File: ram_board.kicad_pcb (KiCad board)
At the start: 2 copper layers, 28.6 x 73 mm, 6 parts, among them J1 Conn_02x20_Odd_Even, J2 Conn_02x05_Odd_Even, U1 IS61LV5128AL-10TLI, U2 SST39VF040-70-4C-NHE

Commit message: Wiring up
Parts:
- added C1: 100nF, Capacitor_SMD:C_0603_1608Metric_Pad1.05x0.95mm_HandSolder, B.Cu at (173.5, 74.8)
- added C2: 100nF, Capacitor_SMD:C_0603_1608Metric_Pad1.05x0.95mm_HandSolder, F.Cu at (142.2, 84.6)
- added C3: 100nF, Capacitor_SMD:C_0603_1608Metric_Pad1.05x0.95mm_HandSolder, F.Cu at (124.1, 90.7)
- added C4: 100uF, Capacitor_SMD:C_1206_3216Metric_Pad1.42x1.75mm_HandSolder, F.Cu at (124.2, 94.0)
- added G***: LOGO, Logos:asian_tiger, F.Cu at (160.8, 85.5)
- added R2: 10K, Resistor_SMD:R_0603_1608Metric_Pad1.05x0.95mm_HandSolder, B.Cu at (177.0, 74.8)
- D1: footprint LED_SMD:LED_0805_2012Metric_Pad1.15x1.40mm_HandSolder -> LED_SMD:LED_0603_1608Metric_Pad1.05x0.95mm_HandSolder
- R1: footprint Resistor_SMD:R_0805_2012Metric_Pad1.15x1.40mm_HandSolder -> Resistor_SMD:R_0603_1608Metric_Pad1.05x0.95mm_HandSolder
- moved U2 39.3 mm to (174.4, 83.9)
- moved U1 38.2 mm to (151.3, 84.1)
- moved J2 30.1 mm to (119.0, 97.5), turned to 90 degrees
- moved J1 18.4 mm to (140.1, 97.7), turned to 90 degrees
- moved R1 11.6 mm to (132.0, 77.0), turned to 180 degrees
- moved D1 4.65 mm to (137.6, 77.0), turned to 180 degrees
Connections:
- J1 pad 1: (no net) -> /A0
- J1 pad 10: (no net) -> /A9
- J1 pad 11: (no net) -> /A10
- J1 pad 12: (no net) -> /A11
- J1 pad 13: (no net) -> /A12
- J1 pad 14: (no net) -> /A13
- J1 pad 15: (no net) -> /A14
- J1 pad 16: (no net) -> /A15
- J1 pad 17: (no net) -> /A16
- J1 pad 18: (no net) -> /A17
- J1 pad 19: (no net) -> /A18
- J1 pad 2: (no net) -> /A1
- J1 pad 21: (no net) -> /RAM_CE
- J1 pad 22: (no net) -> /D0
- J1 pad 23: (no net) -> /RAM_OE
- J1 pad 24: (no net) -> /D1
- J1 pad 25: (no net) -> /RAM_WE
- J1 pad 26: (no net) -> /D2
- J1 pad 28: (no net) -> /D3
- J1 pad 3: (no net) -> /A2
- J1 pad 32: (no net) -> GND
- J1 pad 33: (no net) -> GND
- J1 pad 34: (no net) -> /D4
- J1 pad 36: (no net) -> /D5
- J1 pad 38: (no net) -> /D6
- J1 pad 39: (no net) -> GND
- J1 pad 4: (no net) -> /A3
- J1 pad 40: (no net) -> /D7
- J1 pad 5: (no net) -> /A4
- J1 pad 6: (no net) -> /A5
- J1 pad 7: (no net) -> /A6
- J1 pad 8: (no net) -> /A7
- J1 pad 9: (no net) -> /A8
- J2 pad 10: (no net) -> GND
- J2 pad 3: (no net) -> +3V3
- J2 pad 4: (no net) -> +3V3
- J2 pad 7: (no net) -> GND
- J2 pad 8: (no net) -> GND
- J2 pad 9: (no net) -> GND
- R1 pad 2: (no net) -> +3V3
- U1 pad 10: (no net) -> /D1
- U1 pad 11: Net-(U1-Pad11) -> +3V3
- U1 pad 12: Net-(U1-Pad12) -> GND
- U1 pad 13: (no net) -> /D2
- U1 pad 14: (no net) -> /D3
- U1 pad 15: (no net) -> /RAM_WE
- U1 pad 16: (no net) -> /A5
- U1 pad 17: (no net) -> /A6
- U1 pad 18: (no net) -> /A7
- U1 pad 19: (no net) -> /A8
- U1 pad 20: (no net) -> /A9
- U1 pad 26: (no net) -> /A10
- U1 pad 27: (no net) -> /A11
- U1 pad 28: (no net) -> /A12
- U1 pad 29: (no net) -> /A13
- U1 pad 3: (no net) -> /A0
- U1 pad 30: (no net) -> /A14
- U1 pad 31: (no net) -> /D4
- U1 pad 32: (no net) -> /D5
- U1 pad 33: Net-(U1-Pad11) -> +3V3
- U1 pad 34: Net-(U1-Pad12) -> GND
- U1 pad 35: (no net) -> /D6
- U1 pad 36: (no net) -> /D7
- U1 pad 37: (no net) -> /RAM_OE
- U1 pad 38: (no net) -> /A15
- U1 pad 39: (no net) -> /A16
- U1 pad 4: (no net) -> /A1
- U1 pad 40: (no net) -> /A17
- U1 pad 41: (no net) -> /A18
- U1 pad 5: (no net) -> /A2
- U1 pad 6: (no net) -> /A3
- U1 pad 7: (no net) -> /A4
- U1 pad 8: (no net) -> /RAM_CE
- U1 pad 9: (no net) -> /D0
- U2 pad 1: (no net) -> /A18
- U2 pad 10: (no net) -> /A2
- U2 pad 11: (no net) -> /A1
- U2 pad 12: (no net) -> /A0
- U2 pad 13: (no net) -> /D0
- U2 pad 14: (no net) -> /D1
- U2 pad 15: (no net) -> /D2
- U2 pad 17: (no net) -> /D3
- U2 pad 18: (no net) -> /D4
- U2 pad 19: (no net) -> /D5
- U2 pad 2: (no net) -> /A16
- U2 pad 20: (no net) -> /D6
- U2 pad 21: (no net) -> /D7
- U2 pad 22: (no net) -> /RAM_CE
- U2 pad 23: (no net) -> /A10
- U2 pad 24: (no net) -> /RAM_OE
- U2 pad 25: (no net) -> /A11
- U2 pad 26: (no net) -> /A9
- U2 pad 27: (no net) -> /A8
- U2 pad 28: (no net) -> /A13
- U2 pad 29: (no net) -> /A14
- U2 pad 3: (no net) -> /A15
- U2 pad 30: (no net) -> /A17
- U2 pad 31: (no net) -> Net-(R2-Pad1)
- U2 pad 32: (no net) -> +3V3
- U2 pad 4: (no net) -> /A12
- U2 pad 5: (no net) -> /A7
- U2 pad 6: (no net) -> /A6
- U2 pad 7: (no net) -> /A5
- U2 pad 8: (no net) -> /A4
- U2 pad 9: (no net) -> /A3
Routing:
- added copper zone on B.Cu, net GND
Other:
- board size 28.6 x 73 mm -> 73 x 31.6 mm
- rule trace_min: 0.2 -> 0.1524
- rule via_min_drill: 0.3 -> 0.3302
- rule via_min_size: 0.4 -> 0.6858

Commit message: more cowbell
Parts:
- moved C2 6.38 mm to (148.6, 84.0), turned to 270 degrees
- moved D1 2.17 mm to (135.4, 77.0)
- moved C4 0.22 mm to (124.0, 94.0)
- moved C3 0.11 mm to (124.0, 90.7)
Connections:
- J1 pad 20: (no net) -> Net-(J1-Pad20)
- J1 pad 22: /D0 -> Net-(J1-Pad22)
- J1 pad 24: /D1 -> Net-(J1-Pad24)
- J1 pad 26: /D2 -> Net-(J1-Pad26)
- J1 pad 27: (no net) -> /D0
- J1 pad 28: /D3 -> Net-(J1-Pad28)
- J1 pad 29: (no net) -> /D1
- J1 pad 30: (no net) -> /D2
- J1 pad 31: (no net) -> /D3
- J1 pad 35: (no net) -> /D6
- J1 pad 37: (no net) -> /ROM_CE
- J1 pad 38: /D6 -> /D7
- J1 pad 40: /D7 -> /ROM_OE
- J2 pad 1: (no net) -> Net-(J2-Pad1)
- J2 pad 2: (no net) -> Net-(J2-Pad2)
- J2 pad 5: (no net) -> Net-(J2-Pad5)
- J2 pad 6: (no net) -> Net-(J2-Pad6)
- U1 pad 1: (no net) -> Net-(U1-Pad1)
- U1 pad 2: (no net) -> Net-(U1-Pad2)
- U1 pad 21: (no net) -> Net-(U1-Pad21)
- U1 pad 22: (no net) -> Net-(U1-Pad22)
- U1 pad 23: (no net) -> Net-(U1-Pad23)
- U1 pad 24: (no net) -> Net-(U1-Pad24)
- U1 pad 25: (no net) -> Net-(U1-Pad25)
- U1 pad 42: (no net) -> Net-(U1-Pad42)
- U1 pad 43: (no net) -> Net-(U1-Pad43)
- U1 pad 44: (no net) -> Net-(U1-Pad44)
- U2 pad 22: /RAM_CE -> /ROM_CE
- U2 pad 24: /RAM_OE -> /ROM_OE
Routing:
- net +3V3: track 0.00 -> 101.4 mm, vias 0 -> 2
- net /A3: track 0.00 -> 65.4 mm, vias 0 -> 4
- net /A1: track 0.00 -> 65.1 mm, vias 0 -> 4
- net /A8: track 0.00 -> 64.9 mm, vias 0 -> 4
- net /A9: track 0.00 -> 63.8 mm, vias 0 -> 4
- net /A0: track 0.00 -> 63.2 mm, vias 0 -> 4
- net /A2: track 0.00 -> 61.3 mm, vias 0 -> 4
- net /A4: track 0.00 -> 60.7 mm, vias 0 -> 4
- net /A5: track 0.00 -> 58.7 mm, vias 0 -> 4
- net /A7: track 0.00 -> 58.7 mm, vias 0 -> 4
- net /A6: track 0.00 -> 54.8 mm, vias 0 -> 4
- net /A13: track 0.00 -> 47.7 mm, vias 0 -> 4
- net /A15: track 0.00 -> 45.3 mm, vias 0 -> 4
- net /A11: track 0.00 -> 45.1 mm, vias 0 -> 2
- net /A10: track 0.00 -> 44.4 mm, vias 0 -> 4
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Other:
- rule via_min_drill: 0.3302 -> 0.3048
- rule via_min_size: 0.6858 -> 0.635

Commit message: finished routing, gerbers
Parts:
- C2: moved to B.Cu
- moved G*** 11.5 mm to (149.5, 87.6)
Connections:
- J1 pad 20: Net-(J1-Pad20) -> (no net)
- J1 pad 22: Net-(J1-Pad22) -> (no net)
- J1 pad 24: Net-(J1-Pad24) -> (no net)
- J1 pad 26: Net-(J1-Pad26) -> (no net)
- J1 pad 28: Net-(J1-Pad28) -> (no net)
- J2 pad 1: Net-(J2-Pad1) -> (no net)
- J2 pad 2: Net-(J2-Pad2) -> (no net)
- J2 pad 5: Net-(J2-Pad5) -> (no net)
- J2 pad 6: Net-(J2-Pad6) -> (no net)
- U1 pad 1: Net-(U1-Pad1) -> (no net)
- U1 pad 2: Net-(U1-Pad2) -> (no net)
- U1 pad 21: Net-(U1-Pad21) -> (no net)
- U1 pad 22: Net-(U1-Pad22) -> (no net)
- U1 pad 23: Net-(U1-Pad23) -> (no net)
- U1 pad 24: Net-(U1-Pad24) -> (no net)
- U1 pad 25: Net-(U1-Pad25) -> (no net)
- U1 pad 42: Net-(U1-Pad42) -> (no net)
- U1 pad 43: Net-(U1-Pad43) -> (no net)
- U1 pad 44: Net-(U1-Pad44) -> (no net)
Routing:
- net /D0: track 18.6 -> 53.5 mm, vias 0 -> 2
- net /D3: track 14.5 -> 48.9 mm, vias 0 -> 2
- net /D1: track 18.1 -> 52.2 mm, vias 0 -> 2
- net /D2: track 21.1 -> 54.0 mm, vias 0 -> 2
- net /D5: track 19.5 -> 52.1 mm, vias 0 -> 2
- net /D6: track 18.2 -> 44.1 mm, vias 0 -> 2
- net /D4: track 18.0 -> 43.7 mm, vias 0 -> 2
- net /D7: track 24.5 -> 45.7 mm, vias 1 -> 2
- net /A14: track 29.1 -> 48.2 mm
- net /A17: track 31.0 -> 44.6 mm, vias 2 -> 4
- net /A16: track 29.1 -> 38.9 mm, vias 2 -> 4
- net GND: track 22.7 -> 13.0 mm, vias 7 -> 11
- net /A18: track 30.9 -> 40.4 mm, vias 2 -> 3
- net /A9: track 63.8 -> 71.0 mm
- net /A7: track 58.7 -> 64.0 mm
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- added copper zone on F.Cu, net GND
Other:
- rule via_min_drill: 0.3048 -> 0.254
- rule via_min_size: 0.635 -> 0.508
- board text added: "RL"

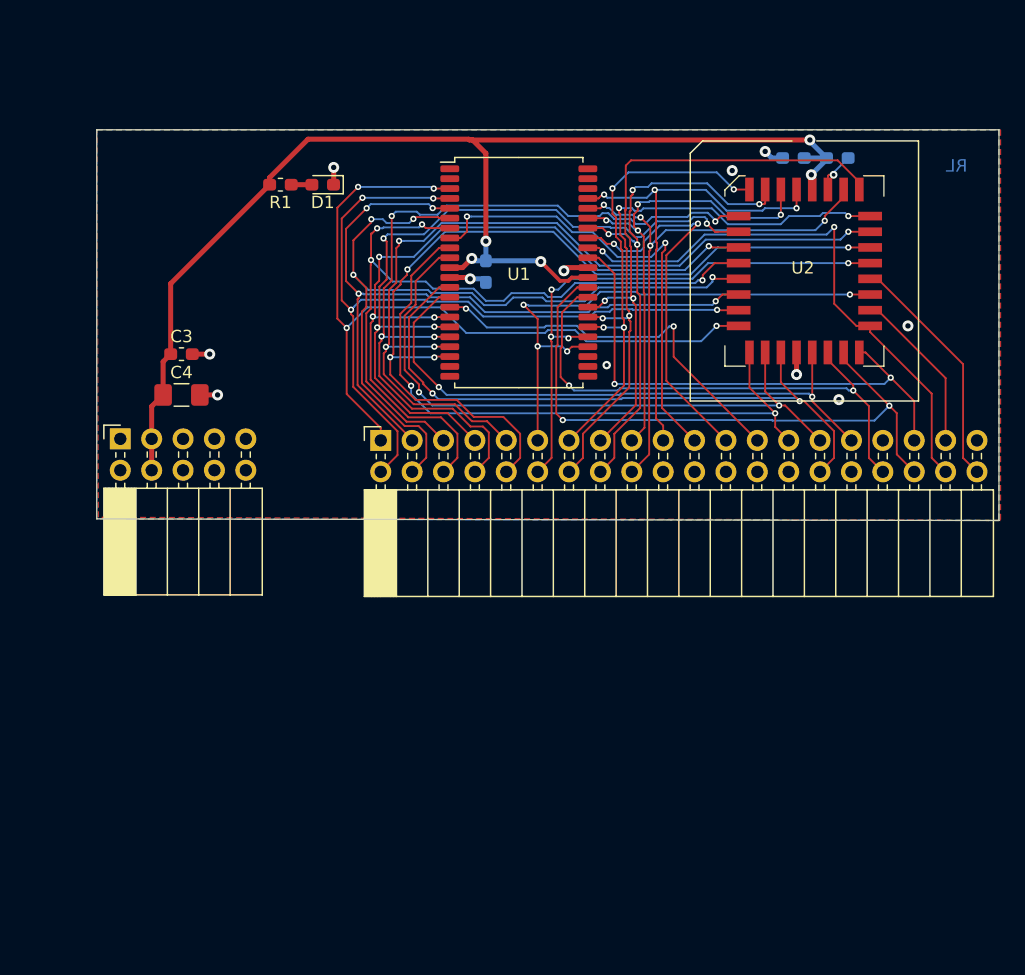
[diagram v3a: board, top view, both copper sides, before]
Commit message: Labeling and status leds
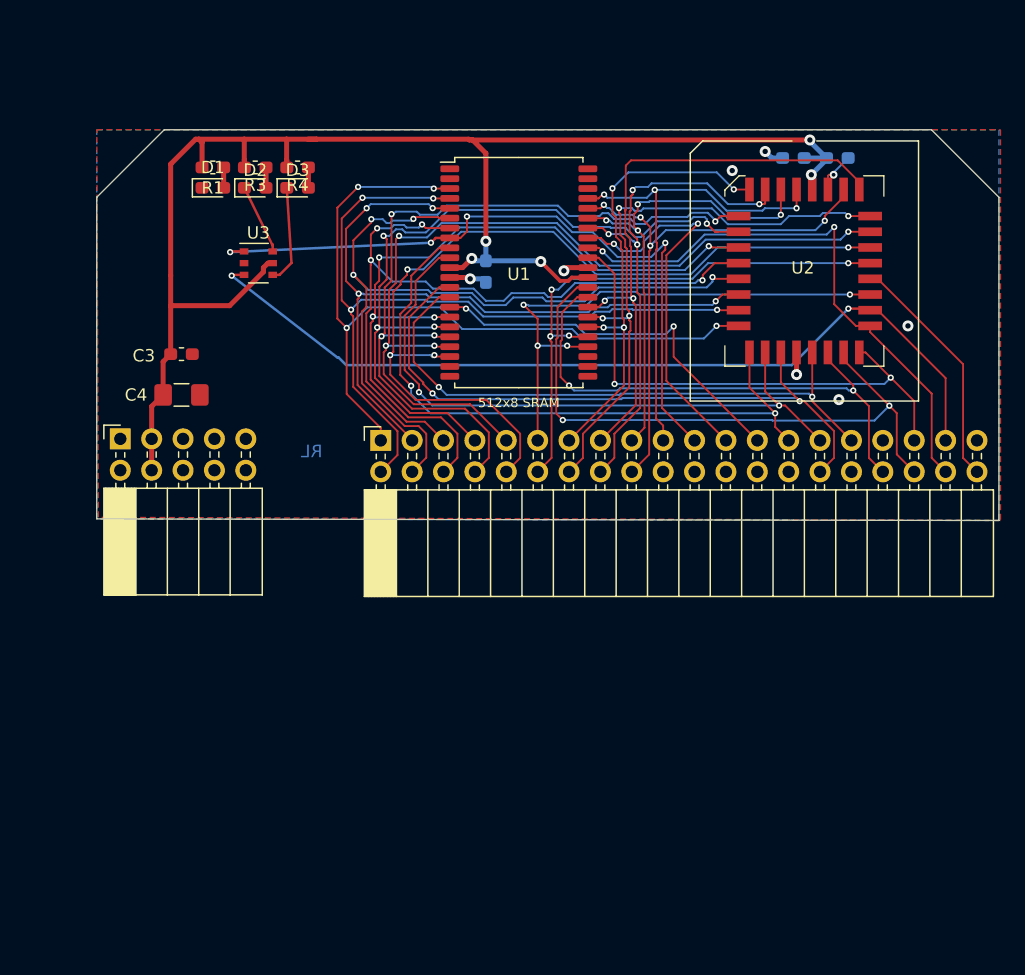
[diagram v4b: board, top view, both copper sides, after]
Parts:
- added D2: LED, LED_SMD:LED_0603_1608Metric_Pad1.05x0.95mm_HandSolder, F.Cu at (129.9, 77.2)
- added D3: LED, LED_SMD:LED_0603_1608Metric_Pad1.05x0.95mm_HandSolder, F.Cu at (133.3, 77.2)
- added R3: 360R, Resistor_SMD:R_0603_1608Metric_Pad1.05x0.95mm_HandSolder, F.Cu at (129.9, 75.6)
- added R4: 360R, Resistor_SMD:R_0603_1608Metric_Pad1.05x0.95mm_HandSolder, F.Cu at (133.3, 75.6)
- added U3: 74LVC2G34, Package_SO:TSOP-6_1.65x3.05mm_P0.95mm, F.Cu at (130.2, 83.3)
- moved G*** 16.1 mm to (133.7, 84.2)
- moved D1 8.89 mm to (126.5, 77.2), turned to 0 degrees
- moved R1 5.65 mm to (126.5, 75.6)
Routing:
- net /ROM_CE: track 13.4 -> 70.6 mm, vias 0 -> 2
- net +3V3: track 102.8 -> 125.6 mm
- net /RAM_CE: track 37.9 -> 57.0 mm, vias 2 -> 4
- net Net-(D3-Pad1): track 0.00 -> 8.01 mm
- net Net-(D2-Pad1): track 0.00 -> 5.78 mm
- net GND: track 13.0 -> 8.78 mm, vias 11 -> 7
- net Net-(D3-Pad2): track 0.00 -> 1.65 mm
- net Net-(D2-Pad2): track 0.00 -> 1.65 mm
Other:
- outline, holes or cut-outs redrawn
- board text added: "512x8 SRAM"
- board text added: "DeltaBrd RAM/ROM Extension v1.0 © 2019 by Hyiger Designs DeltaBrd © Dr. Svetozar Ilchev http://ilchev.net/deltabrd"

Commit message: Final Version
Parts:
- added R5: 360R, Resistor_SMD:R_0603_1608Metric_Pad1.05x0.95mm_HandSolder, F.Cu at (133.1, 78.0)
- added R6: 360R, Resistor_SMD:R_0603_1608Metric_Pad1.05x0.95mm_HandSolder, F.Cu at (133.1, 74.9)
- D2: value LED -> RAM Enabled; footprint LED_SMD:LED_0603_1608Metric_Pad1.05x0.95mm_HandSolder -> LED_SMD:LED_2C_0603_1608Metric_Pad1.05x0.95mm_HandSolder
- D3: value LED -> ROM Enabled; footprint LED_SMD:LED_0603_1608Metric_Pad1.05x0.95mm_HandSolder -> LED_SMD:LED_2C_0603_1608Metric_Pad1.05x0.95mm_HandSolder
- R1: value R_Small -> 360R
- U3: value 74LVC2G34 -> 74LVC04ADR; footprint Package_SO:TSOP-6_1.65x3.05mm_P0.95mm -> Package_SO:SSOP-14_5.3x6.2mm_P0.65mm
- moved R4 3.86 mm to (129.5, 74.9)
- moved R1 2.47 mm to (126.0, 78.0)
- moved R3 2.44 mm to (129.5, 78.0)
- moved U3 2.13 mm to (129.5, 85.3)
- moved D1 0.92 mm to (126.0, 76.5)
- moved D2 0.85 mm to (129.5, 76.5)
- moved D3 0.80 mm to (133.1, 76.5)
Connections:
- R3 pad 1: Net-(D2-Pad2) -> Net-(D2-Pad3)
- R4 pad 1: Net-(D3-Pad2) -> Net-(D2-Pad1)
- U3 pad 2: GND -> Net-(D2-Pad4)
- U3 pad 3: /ROM_CE -> Net-(D2-Pad4)
- U3 pad 4: Net-(D3-Pad1) -> Net-(D2-Pad2)
- U3 pad 5: +3V3 -> /ROM_CE
- U3 pad 6: Net-(D2-Pad1) -> Net-(D3-Pad4)
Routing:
- net Net-(D3-Pad4): track 0.00 -> 18.3 mm, vias 0 -> 2
- net Net-(D3-Pad2): track 1.65 -> 14.3 mm
- net Net-(D2-Pad4): track 0.00 -> 10.5 mm
- net Net-(D2-Pad2): track 1.65 -> 11.8 mm
- net GND: track 8.78 -> 18.7 mm, vias 7 -> 16
- net Net-(D3-Pad1): track 8.01 -> 1.20 mm
- net Net-(D2-Pad1): track 5.78 -> 1.20 mm
- net /A14: track 48.2 -> 44.1 mm, vias 2 -> 4
- net +3V3: track 125.6 -> 128.0 mm, vias 5 -> 9
- net /RAM_CE: track 57.0 -> 58.4 mm
- net Net-(D3-Pad3): track 0.00 -> 1.22 mm
- net Net-(D2-Pad3): track 0.00 -> 1.22 mm
- net /D7: track 45.8 -> 44.6 mm
- net /ROM_CE: track 70.6 -> 71.4 mm
- net /A8: track 70.5 -> 71.3 mm
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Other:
- board text added: "512Kx8 ROM"
- board text added: "512Kx8 SRAM"
- board text added: "PWR"
- board text added: "RAM ENA"
- board text added: "ROM ENA"
- board text removed: "512x8 SRAM"

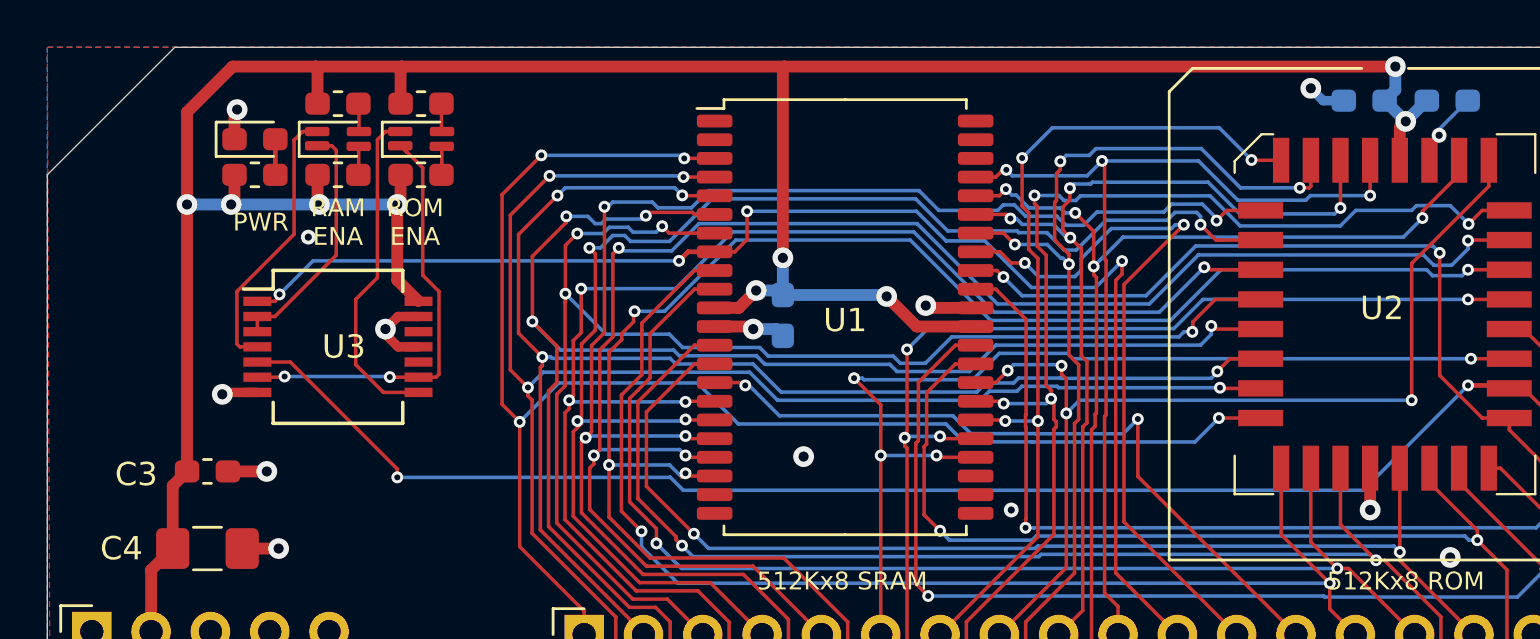
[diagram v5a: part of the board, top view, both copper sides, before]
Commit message: added BOM and schema docs
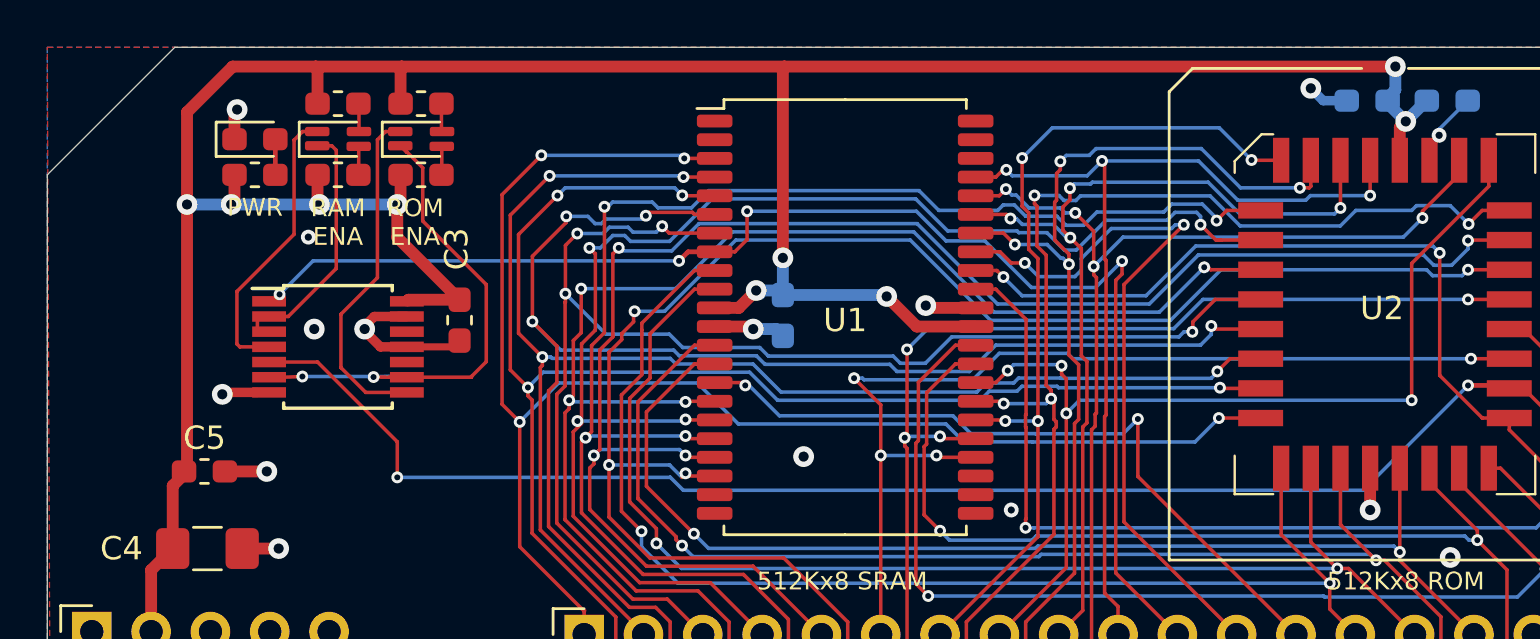
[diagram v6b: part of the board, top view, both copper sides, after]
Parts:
- added C5: 100nF, Capacitor_SMD:C_0603_1608Metric_Pad1.05x0.95mm_HandSolder, F.Cu at (123.8, 90.7)
- D2: value RAM Enabled -> LED
- D3: value ROM Enabled -> LED
- U3: value 74LVC04ADR -> 74LVC04A; footprint Package_SO:SSOP-14_5.3x6.2mm_P0.65mm -> Package_SO:TSSOP-14_4.4x5mm_P0.65mm
- moved C3 12.6 mm to (134.7, 84.2), turned to 270 degrees
- moved C1 0.13 mm to (173.6, 74.8)
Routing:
- net GND: track 18.7 -> 23.5 mm, vias 16 -> 17
- net Net-(D3-Pad4): track 18.3 -> 22.2 mm
- net +3V3: track 128.0 -> 130.9 mm
- net Net-(D3-Pad2): track 14.3 -> 15.3 mm
- net /ROM_CE: track 71.4 -> 72.1 mm
